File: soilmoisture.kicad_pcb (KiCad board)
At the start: 2 copper layers, 33 x 99.1 mm, 9 parts, among them J1 Conn_ARM_JTAG_SWD_10, U1 BT840, U2 BAT-HLD-001, Y1 32KHZ

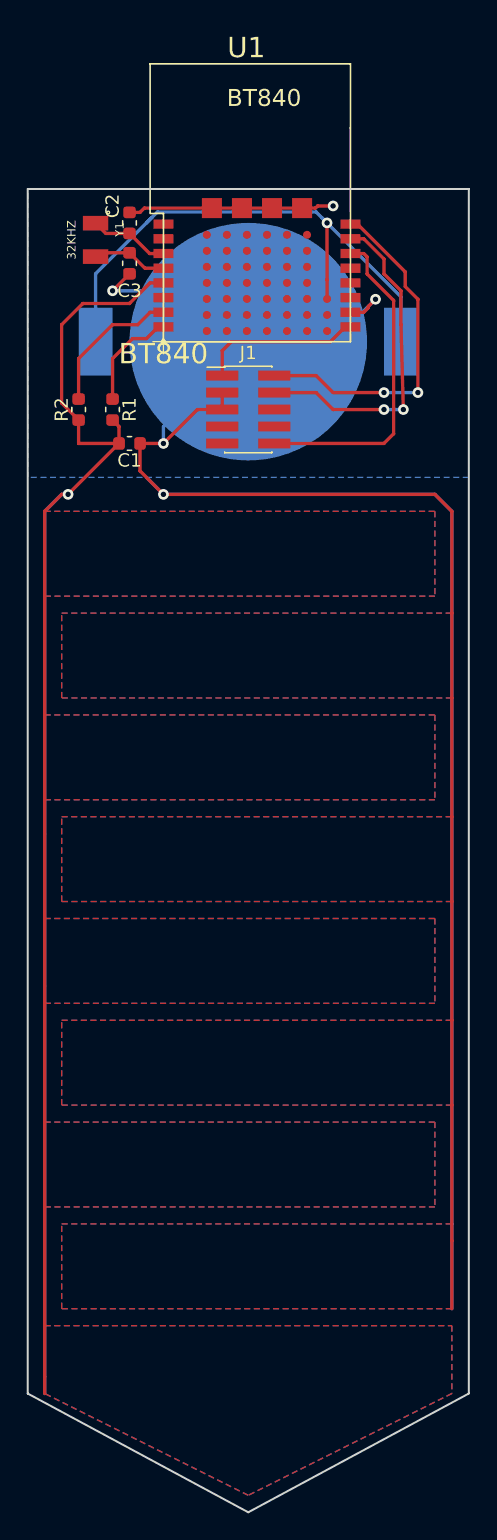
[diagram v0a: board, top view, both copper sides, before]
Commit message: Feat: Four layer pcb, added NTC
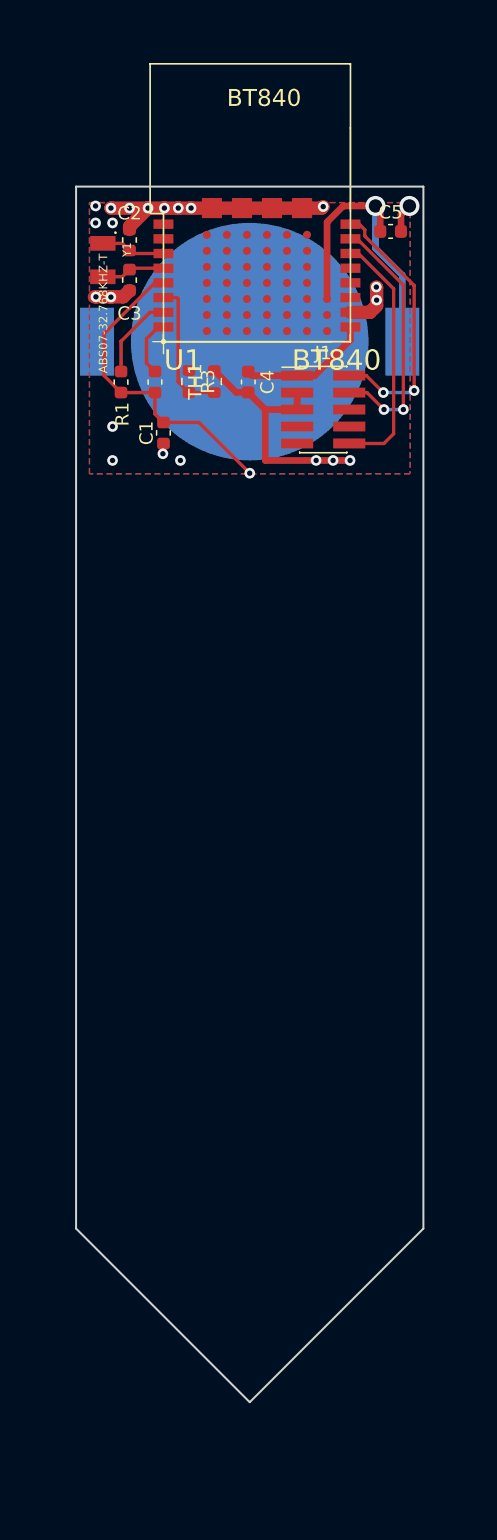
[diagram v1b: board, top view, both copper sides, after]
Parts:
- added C4: 4.7uf, Capacitor_SMD:C_0603_1608Metric, F.Cu at (135.9, 57.6)
- added C5: 4.7uf, Capacitor_SMD:C_0603_1608Metric, F.Cu at (146.5, 46.4)
- added R3: 100k, Resistor_SMD:R_0603_1608Metric, F.Cu at (131.4, 57.6)
- added TH1: Thermistor_NTC, Resistor_SMD:R_0603_1608Metric, F.Cu at (133.3, 57.6)
- Y1: value 32KHZ -> ABS07-32.768KHZ-T
- moved J1 5.61 mm to (141.5, 59.7)
- moved R1 3.78 mm to (126.4, 57.6)
- moved R2 3.78 mm to (128.9, 57.6)
- moved C1 2.66 mm to (129.5, 61.4), turned to -90 degrees
- moved Y1 1.60 mm to (125.0, 48.5)
- moved C2 1.28 mm to (127.0, 47.0)
- moved C3 1.26 mm to (127.0, 50.0)
- moved U2 0.11 mm to (136.0, 54.6)
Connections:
- J1 pad 6: Net-(J1-Pad6) -> unconnected-(J1-SWO/TDO-Pad6)
- J1 pad 7: Net-(J1-Pad7) -> unconnected-(J1-KEY-Pad7)
- J1 pad 8: Net-(J1-Pad8) -> unconnected-(J1-NC/TDI-Pad8)
- J1 pad 9: Net-(J1-Pad9) -> unconnected-(J1-GNDDetect-Pad9)
- U1 pad P$1: Net-(U1-PadP$1) -> unconnected-(U1-P26/SDA-PadP$1)
- U1 pad P$11: Net-(U1-PadP$11) -> unconnected-(U1-P13-PadP$11)
- U1 pad P$12: Net-(U1-PadP$12) -> unconnected-(U1-P18-PadP$12)
- U1 pad P$13: Net-(U1-PadP$13) -> unconnected-(U1-P20-PadP$13)
- U1 pad P$2: Net-(U1-PadP$2) -> unconnected-(U1-P27/SCL-PadP$2)
- U1 pad P$6: Net-(U1-PadP$6) -> /NTC
- U1 pad P$A0: Net-(U1-PadP$A0) -> unconnected-(U1-A0/VSS1-PadP$A0)
- U1 pad P$A1: Net-(U1-PadP$A1) -> unconnected-(U1-A1/P28-PadP$A1)
- U1 pad P$A2: Net-(U1-PadP$A2) -> unconnected-(U1-A2/P29-PadP$A2)
- U1 pad P$A3: Net-(U1-PadP$A3) -> unconnected-(U1-A3/P04-PadP$A3)
- U1 pad P$A4: Net-(U1-PadP$A4) -> unconnected-(U1-A4/P05-PadP$A4)
- U1 pad P$A5: Net-(U1-PadP$A5) -> unconnected-(U1-A5/P07-PadP$A5)
- U1 pad P$A6: Net-(U1-PadP$A6) -> unconnected-(U1-A6/P108-PadP$A6)
- U1 pad P$B0: Net-(U1-PadP$B0) -> unconnected-(U1-B0/VSS2-PadP$B0)
- U1 pad P$B1: Net-(U1-PadP$B1) -> unconnected-(U1-B1/P25-PadP$B1)
- U1 pad P$B2: Net-(U1-PadP$B2) -> unconnected-(U1-B2/P30-PadP$B2)
- U1 pad P$B3: Net-(U1-PadP$B3) -> unconnected-(U1-B3/P31-PadP$B3)
- U1 pad P$B4: Net-(U1-PadP$B4) -> unconnected-(U1-B4/NC-PadP$B4)
- U1 pad P$B5: Net-(U1-PadP$B5) -> unconnected-(U1-B5/P08-PadP$B5)
- U1 pad P$B6: Net-(U1-PadP$B6) -> unconnected-(U1-B6/P103-PadP$B6)
- U1 pad P$C0: Net-(U1-PadP$C0) -> unconnected-(U1-C0/VSS3-PadP$C0)
- U1 pad P$C1: Net-(U1-PadP$C1) -> unconnected-(U1-C1/P24-PadP$C1)
- U1 pad P$C2: Net-(U1-PadP$C2) -> unconnected-(U1-C2/P22-PadP$C2)
- U1 pad P$C3: Net-(U1-PadP$C3) -> unconnected-(U1-C3/NC-PadP$C3)
- U1 pad P$C4: Net-(U1-PadP$C4) -> unconnected-(U1-C4/P15-PadP$C4)
- U1 pad P$C5: Net-(U1-PadP$C5) -> unconnected-(U1-C5/P12-PadP$C5)
- U1 pad P$C6: Net-(U1-PadP$C6) -> unconnected-(U1-C6/P104-PadP$C6)
- U1 pad P$D0: Net-(U1-PadP$D0) -> unconnected-(U1-D0/VSS4-PadP$D0)
- U1 pad P$D1: Net-(U1-PadP$D1) -> unconnected-(U1-D1/P23-PadP$D1)
- U1 pad P$D2: Net-(U1-PadP$D2) -> unconnected-(U1-D2/NC-PadP$D2)
- U1 pad P$D3: Net-(U1-PadP$D3) -> unconnected-(U1-D3/P16-PadP$D3)
- U1 pad P$D4: Net-(U1-PadP$D4) -> unconnected-(U1-D4/P14-PadP$D4)
- U1 pad P$D5: Net-(U1-PadP$D5) -> unconnected-(U1-D5/P11-PadP$D5)
- U1 pad P$D6: Net-(U1-PadP$D6) -> unconnected-(U1-D6/P105-PadP$D6)
- U1 pad P$E0: Net-(U1-PadP$E0) -> unconnected-(U1-E0/P107-PadP$E0)
- U1 pad P$E1: Net-(U1-PadP$E1) -> unconnected-(U1-E1/P20-PadP$E1)
- U1 pad P$E2: Net-(U1-PadP$E2) -> unconnected-(U1-E2/P21-PadP$E2)
- U1 pad P$E3: Net-(U1-PadP$E3) -> unconnected-(U1-E3/P109-PadP$E3)
- U1 pad P$E4: Net-(U1-PadP$E4) -> unconnected-(U1-E4/D+-PadP$E4)
- U1 pad P$E5: Net-(U1-PadP$E5) -> unconnected-(U1-E5/D--PadP$E5)
- U1 pad P$E6: Net-(U1-PadP$E6) -> unconnected-(U1-E6/P12-PadP$E6)
- U1 pad P$F5: Net-(U1-PadP$F5) -> unconnected-(U1-F5/DCCH-PadP$F5)
- U1 pad P$F6: Net-(U1-PadP$F6) -> unconnected-(U1-F6/VBUS-PadP$F6)
- U1 pad P$Z0: Net-(U1-PadP$Z0) -> unconnected-(U1-Z0/P111-PadP$Z0)
- U1 pad P$Z1: Net-(U1-PadP$Z1) -> unconnected-(U1-Z1/P112-PadP$Z1)
- U1 pad P$Z2: Net-(U1-PadP$Z2) -> unconnected-(U1-Z2/P113-PadP$Z2)
- U1 pad P$Z3: Net-(U1-PadP$Z3) -> unconnected-(U1-Z3/P114-PadP$Z3)
- U1 pad P$Z4: Net-(U1-PadP$Z4) -> unconnected-(U1-Z4/P115-PadP$Z4)
- U1 pad P$Z5: Net-(U1-PadP$Z5) -> unconnected-(U1-Z5/P110-PadP$Z5)
- U1 pad P$Z6: Net-(U1-PadP$Z6) -> unconnected-(U1-Z6/P106-PadP$Z6)
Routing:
- net GND: track 224.5 -> 51.0 mm, vias 5 -> 19
- net /SOIL_READ: track 165.3 -> 85.4 mm
- net +BATT: track 42.7 -> 22.9 mm
- net /NTC: track 0.00 -> 10.4 mm
- net /SWDIO: track 26.3 -> 20.3 mm
- net /nRST: track 24.7 -> 18.8 mm
- net /SWDCLK: track 25.3 -> 19.5 mm
- net /CAP_CHARGE: track 10.8 -> 6.34 mm
- net /CAP_DISCHARGE: track 7.81 -> 4.35 mm
- net VDD: track 12.2 -> 9.84 mm
- net /XL1: track 6.60 -> 5.40 mm
- net Net-(J1-Pad7): track 0.83 -> 0.00 mm
- net (no net): vias 0 -> 3
- added copper zone on In1.Cu, net GND
- added copper zone on In2.Cu, net GND
- removed copper zone on B.Cu, net /SOIL_READ
- removed copper zone on F.Cu, net /SOIL_READ
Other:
- board size 33 x 99.1 mm -> 26 x 91 mm
- copper layers 2 -> 4
- net class Default removed

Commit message: Feat: Memsic oscillator and schmitt buffer, dual probes
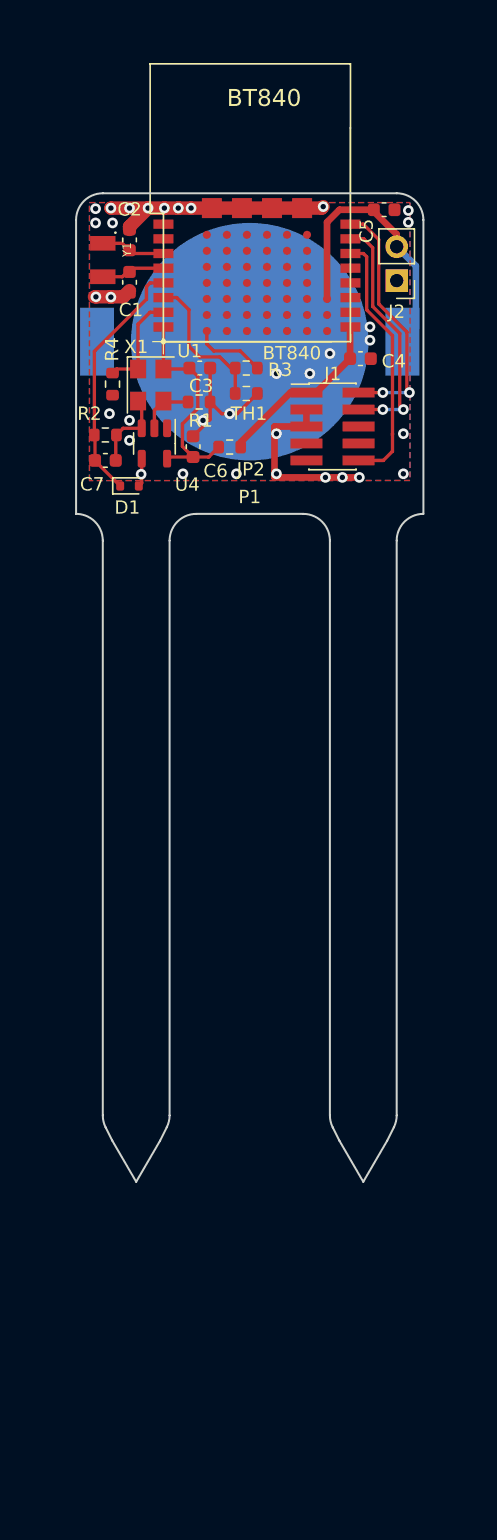
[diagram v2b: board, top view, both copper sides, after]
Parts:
- added C6: 100nF, Capacitor_SMD:C_0603_1608Metric, F.Cu at (131.8, 62.5)
- added C7: 100nF, Capacitor_SMD:C_0603_1608Metric, F.Cu at (125.2, 63.5)
- added D1: CDSU101A, Diode_SMD:D_SOD-523, F.Cu at (127.0, 65.4)
- added J2: Conn_01x02, Connector_PinHeader_2.54mm:PinHeader_1x02_P2.54mm_Vertical, F.Cu at (147.0, 50.0)
- added JP2: 0R, Resistor_SMD:R_0603_1608Metric, F.Cu at (134.5, 62.5)
- added P1: 1-30pf, soil_lib:1-30pf_Soil_Probe, F.Cu at (136.0, 91.0)
- added R4: 100k, Resistor_SMD:R_0603_1608Metric, F.Cu at (125.7, 57.8)
- added U4: SN74LVC1G14DBV, Package_TO_SOT_SMD:SOT-23-5, F.Cu at (128.9, 62.2)
- added X1: SIT8008BC-23-18E-80.000000, Oscillator:Oscillator_SMD_SeikoEpson_SG8002CE-4Pin_3.2x2.5mm, F.Cu at (128.6, 57.9)
- C1: value C_Variable -> 12pF
- C3: value 12pF -> 100nF
- R2: value 220 -> 100k
- moved C1 11.6 mm to (127.0, 50.2), turned to 90 degrees
- moved C4 8.58 mm to (144.3, 55.9), turned to 0 degrees
- moved C3 8.43 mm to (132.3, 56.6), turned to 0 degrees
- moved R1 6.03 mm to (132.2, 59.1), turned to 0 degrees
- moved R2 5.43 mm to (125.2, 61.6), turned to 0 degrees
- moved R3 4.41 mm to (135.7, 56.6), turned to 180 degrees
- moved TH1 2.55 mm to (135.7, 58.5), turned to 0 degrees
- moved C5 1.69 mm to (146.1, 44.7)
- moved J1 1.45 mm to (142.2, 61.0)
- turned C2 to -90 degrees
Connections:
- net /NTC renamed NTC_ADC
- C1 pad 1: /SOIL_READ -> GND
- C1 pad 2: GND -> /XL2
- C2 pad 1: /XL1 -> GND
- C2 pad 2: GND -> /XL1
- C3 pad 1: /XL2 -> /Oscillator/gpio_power
- R1 pad 1: /CAP_CHARGE -> Net-(X1-OUT)
- R1 pad 2: /SOIL_READ -> GND
- R2 pad 1: /SOIL_READ -> /Oscillator/ADC_OUT
- R2 pad 2: /CAP_DISCHARGE -> GND
- R3 pad 1: unconnected-(R3-Pad1) -> /NTC_POWER
- U1 pad P$5: /SOIL_READ -> /Oscillator/ADC_OUT
- U1 pad P$7: /CAP_CHARGE -> /Oscillator/enable
- U1 pad P$8: /CAP_DISCHARGE -> /Oscillator/gpio_power
- U1 pad P$Z6: unconnected-(U1-Z6/P106-PadP$Z6) -> /NTC_POWER
- U2 pad +@1: +BATT -> (no net)
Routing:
- net /SOIL_READ: track 85.4 -> 0.00 mm, vias 1 -> 0
- net /Oscillator/Probe: track 0.00 -> 28.0 mm, vias 0 -> 1
- net GND: track 51.0 -> 77.1 mm, vias 19 -> 33
- net /Oscillator/ADC_OUT: track 0.00 -> 18.7 mm
- net /Oscillator/gpio_power: track 0.00 -> 17.1 mm
- net /Oscillator/enable: track 0.00 -> 7.66 mm
- net /CAP_CHARGE: track 6.34 -> 0.00 mm
- net /NTC_POWER: track 0.00 -> 5.50 mm
- net /CAP_DISCHARGE: track 4.35 -> 0.00 mm
- net Net-(X1-OUT): track 0.00 -> 4.19 mm
- net VDD: track 9.84 -> 13.5 mm
- net +BATT: track 22.9 -> 21.2 mm, vias 1 -> 0
- net /SWDIO: track 20.3 -> 18.8 mm
- net /SWDCLK: track 19.5 -> 18.5 mm
- net /nRST: track 18.8 -> 19.6 mm
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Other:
- board size 26 x 91 mm -> 26 x 74 mm
